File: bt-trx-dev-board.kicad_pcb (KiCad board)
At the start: 2 copper layers, 78 x 68 mm, 59 parts, among them J1 RJ45, J10 JMP_CON_TRX, J11 VOX_IN, J12 VOX_TRX, J2 PTT_BUTTON, J3 PTT_CON, J5 PTT_SEL, J6 I2C, J7 SW1_CON, J8 I2C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

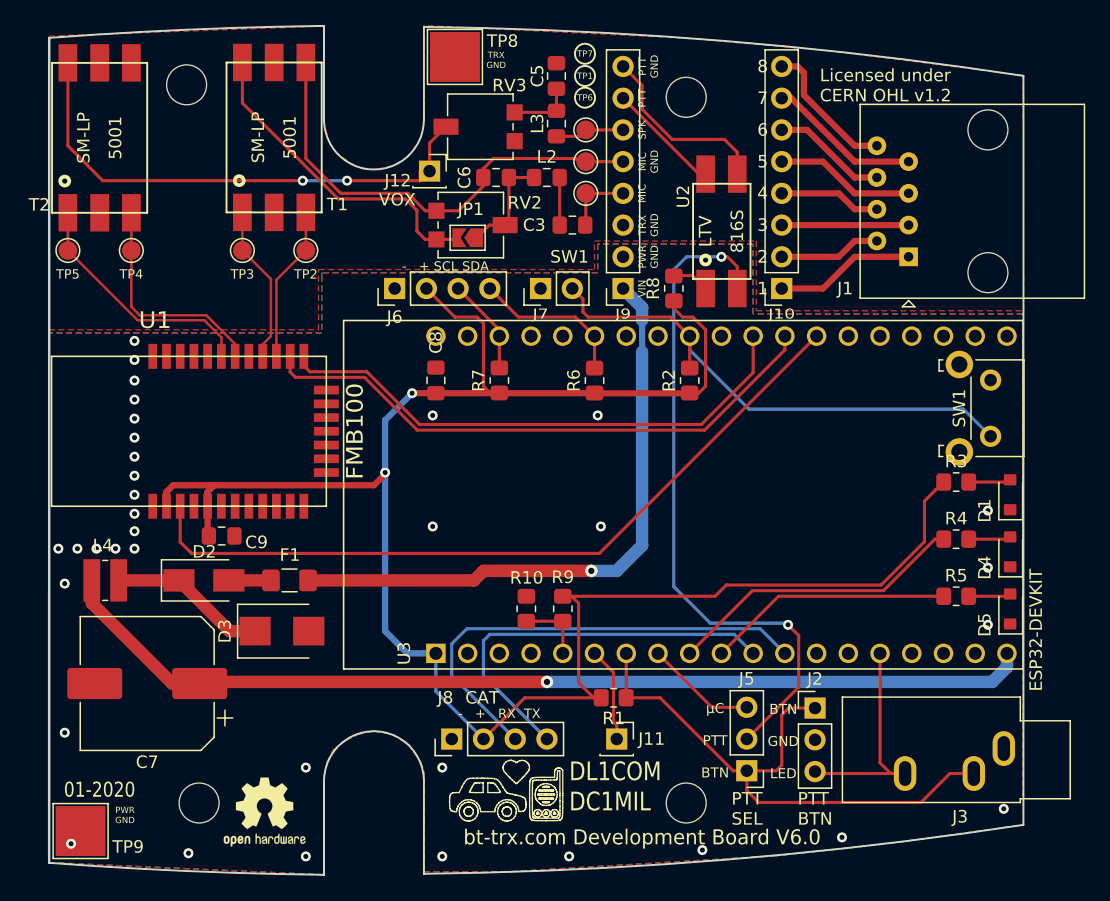
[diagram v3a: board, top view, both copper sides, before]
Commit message: am: Connected FMB100 RST pin to ESP
* Connected FMB100 RST pin to ESP in schematic and PCB
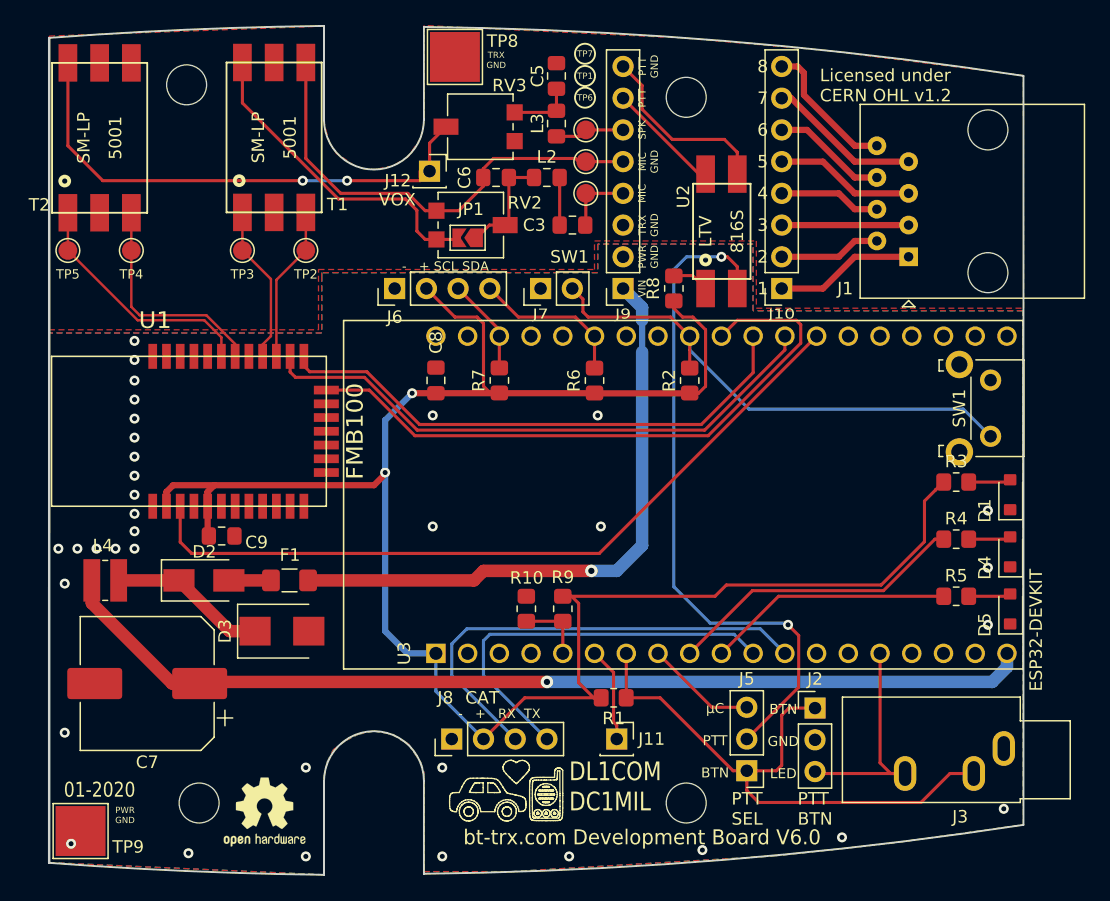
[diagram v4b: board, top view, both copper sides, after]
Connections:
- net /WT32_ONOFF_FROM_UC renamed /FMB_ONOFF_FROM_UC
- U1 pad 19: unconnected-(U1-Pad19) -> /FMB_RST_FROM_UC
- U3 pad 29: unconnected-(U3-Pad29) -> /FMB_RST_FROM_UC
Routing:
- net /FMB_RST_FROM_UC: track 0.00 -> 51.1 mm
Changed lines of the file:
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@@
   (net 2 "+3V3")
   (net 3 "+5V")
-  (net 4 "/WT32_ONOFF_FROM_UC")
+  (net 4 "/FMB_ONOFF_FROM_UC")
   (net 5 "/UART_UC_TX")
   (net 6 "/UART_UC_RX")
@@
   (net 61 "unconnected-(U1-Pad17)")
   (net 62 "unconnected-(U1-Pad18)")
-  (net 63 "unconnected-(U1-Pad19)")
+  (net 63 "/FMB_RST_FROM_UC")
   (net 64 "unconnected-(U1-Pad27)")
   (net 65 "unconnected-(U1-Pad28)")
@@
   (net 75 "unconnected-(U3-Pad24)")
   (net 76 "unconnected-(U3-Pad27)")
-  (net 77 "unconnected-(U3-Pad29)")
-  (net 78 "unconnected-(U3-Pad33)")
-  (net 79 "unconnected-(U3-Pad34)")
-  (net 80 "unconnected-(U3-Pad35)")
-  (net 81 "unconnected-(U3-Pad36)")
-  (net 82 "unconnected-(U3-Pad37)")
-  (net 83 "unconnected-(U3-Pad38)")
-  (net 84 "unconnected-(U1-Pad24)")
+  (net 77 "unconnected-(U3-Pad33)")
+  (net 78 "unconnected-(U3-Pad34)")
+  (net 79 "unconnected-(U3-Pad35)")
+  (net 80 "unconnected-(U3-Pad36)")
+  (net 81 "unconnected-(U3-Pad37)")
+  (net 82 "unconnected-(U3-Pad38)")
+  (net 83 "unconnected-(U1-Pad24)")
   (footprint "MountingHole:MountingHole_3.2mm_M3_DIN965" (layer "F.Cu")
     (at 171.425 127.55)
@@
       (net 10 "/Microcontroller/BTN0") (pinfunction "IO18") (pintype "bidirectional"))
     (pad "29" thru_hole circle locked (at 12.7 3.1 90) (size 1.56 1.56) (drill 1.04) (layers *.Cu *.Mask)
-      (net 77 "unconnected-(U3-Pad29)") (pinfunction "IO5") (pintype "bidirectional+no_connect"))
+      (net 63 "/FMB_RST_FROM_UC") (pinfunction "IO5") (pintype "bidirectional"))
     (pad "30" thru_hole circle locked (at 12.7 5.64 90) (size 1.56 1.56) (drill 1.04) (layers *.Cu *.Mask)
       (net 5 "/UART_UC_TX") (pinfunction "IO17") (pintype "bidirectional"))
@@
       (net 6 "/UART_UC_RX") (pinfunction "IO16") (pintype "bidirectional"))
     (pad "32" thru_hole circle locked (at 12.7 10.72 90) (size 1.56 1.56) (drill 1.04) (layers *.Cu *.Mask)
-      (net 4 "/WT32_ONOFF_FROM_UC") (pinfunction "IO4") (pintype "bidirectional"))
+      (net 4 "/FMB_ONOFF_FROM_UC") (pinfunction "IO4") (pintype "bidirectional"))
     (pad "33" thru_hole circle locked (at 12.7 13.26 90) (size 1.56 1.56) (drill 1.04) (layers *.Cu *.Mask)
-      (net 78 "unconnected-(U3-Pad33)") (pinfunction "IO0") (pintype "bidirectional+no_connect"))
+      (net 77 "unconnected-(U3-Pad33)") (pinfunction "IO0") (pintype "bidirectional+no_connect"))
     (pad "34" thru_hole circle locked (at 12.7 15.8 90) (size 1.56 1.56) (drill 1.04) (layers *.Cu *.Mask)
-      (net 79 "unconnected-(U3-Pad34)") (pinfunction "IO2") (pintype "bidirectional+no_connect"))
+      (net 78 "unconnected-(U3-Pad34)") (pinfunction "IO2") (pintype "bidirectional+no_connect"))
     (pad "35" thru_hole circle locked (at 12.7 18.34 90) (size 1.56 1.56) (drill 1.04) (layers *.Cu *.Mask)
-      (net 80 "unconnected-(U3-Pad35)") (pinfunction "IO15") (pintype "bidirectional+no_connect"))
+      (net 79 "unconnected-(U3-Pad35)") (pinfunction "IO15") (pintype "bidirectional+no_connect"))
     (pad "36" thru_hole circle locked (at 12.7 20.88 90) (size 1.56 1.56) (drill 1.04) (layers *.Cu *.Mask)
-      (net 81 "unconnected-(U3-Pad36)") (pinfunction "SD1") (pintype "bidirectional+no_connect"))
+      (net 80 "unconnected-(U3-Pad36)") (pinfunction "SD1") (pintype "bidirectional+no_connect"))
     (pad "37" thru_hole circle locked (at 12.7 23.42 90) (size 1.56 1.56) (drill 1.04) (layers *.Cu *.Mask)
-      (net 82 "unconnected-(U3-Pad37)") (pinfunction "SD0") (pintype "bidirectional+no_connect"))
+      (net 81 "unconnected-(U3-Pad37)") (pinfunction "SD0") (pintype "bidirectional+no_connect"))
     (pad "38" thru_hole circle locked (at 12.7 25.96 90) (size 1.56 1.56) (drill 1.04) (layers *.Cu *.Mask)
-      (net 83 "unconnected-(U3-Pad38)") (pinfunction "CLK") (pintype "input+no_connect"))
+      (net 82 "unconnected-(U3-Pad38)") (pinfunction "CLK") (pintype "input+no_connect"))
   )
   (footprint "Capacitor_SMD:CP_Elec_10x10.5" (layer "F.Cu")
@@
       (net 2 "+3V3") (pinfunction "VBAT") (pintype "power_in"))
     (pad "3" smd rect locked (at -11.7 0) (size 0.7 2) (layers "F.Cu" "F.Paste" "F.Mask")
-      (net 4 "/WT32_ONOFF_FROM_UC") (pinfunction "VREG_EN") (pintype "bidirectional"))
+      (net 4 "/FMB_ONOFF_FROM_UC") (pinfunction "VREG_EN") (pintype "bidirectional"))
     (pad "4" smd rect locked (at -10.6 0) (size 0.7 2) (layers "F.Cu" "F.Paste" "F.Mask")
       (net 50 "unconnected-(U1-Pad4)") (pinfunction "PIO16") (pintype "bidirectional+no_connect"))
@@
       (net 62 "unconnected-(U1-Pad18)") (pinfunction "PIO3") (pintype "bidirectional+no_connect"))
     (pad "19" smd rect locked (at 0 -9.3 90) (size 0.7 2) (layers "F.Cu" "F.Paste" "F.Mask")
-      (net 63 "unconnected-(U1-Pad19)") (pinfunction "PIO1/RSTN") (pintype "bidirectional+no_connect"))
+      (net 63 "/FMB_RST_FROM_UC") (pinfunction "PIO1/RSTN") (pintype "bidirectional"))
     (pad "20" smd rect locked (at -1.8 -12) (size 0.7 2) (layers "F.Cu" "F.Paste" "F.Mask")
       (net 5 "/UART_UC_TX") (pinfunction "UART_RX") (pintype "bidirectional"))
@@
       (net 24 "/A_OUT_LP") (pinfunction "SPK_P") (pintype "passive"))
     (pad "24" smd rect locked (at -6.2 -12) (size 0.7 2) (layers "F.Cu" "F.Paste" "F.Mask")
-      (net 84 "unconnected-(U1-Pad24)") (pinfunction "MIC_BIAS") (pintype "power_out+no_connect"))
+      (net 83 "unconnected-(U1-Pad24)") (pinfunction "MIC_BIAS") (pintype "power_out+no_connect"))
     (pad "25" smd rect locked (at -7.3 -12) (size 0.7 2) (layers "F.Cu" "F.Paste" "F.Mask")
       (net 25 "/A_IN_LN") (pinfunction "MIC1_N") (pintype "passive"))
@@
   (segment (start 161.544 112.998) (end 161.544 115.57) (width 0.25) (layer "F.Cu") (net 49))
   (segment (start 158.623 112.998) (end 161.544 112.998) (width 0.25) (layer "F.Cu") (net 49))
+  (segment (start 175.514 88.9) (end 180.2384 88.9) (width 0.25) (layer "F.Cu") (net 63))
+  (segment (start 174.244 90.17) (end 175.514 88.9) (width 0.25) (layer "F.Cu") (net 63))
+  (segment (start 180.2384 88.9) (end 180.594 89.2556) (width 0.25) (layer "F.Cu") (net 63))
+  (segment (start 149.704208 98.145) (end 146.049208 94.49) (width 0.25) (layer "F.Cu") (net 63))
+  (segment (start 180.594 90.7288) (end 173.1778 98.145) (width 0.25) (layer "F.Cu") (net 63))
+  (segment (start 146.049208 94.49) (end 142.6112 94.49) (width 0.25) (layer "F.Cu") (net 63))
+  (segment (start 180.594 89.2556) (end 180.594 90.7288) (width 0.25) (layer "F.Cu") (net 63))
+  (segment (start 173.1778 98.145) (end 149.704208 98.145) (width 0.25) (layer "F.Cu") (net 63))
   (zone (net 28) (net_name "GNDPWR") (layer "F.Cu") (hatch edge 0.508)
     (connect_pads (clearance 0.2))
@@
     (polygon
       (pts
-        (xy 198.374 88.392)
-        (xy 176.784 88.392)
+        (xy 198.374 88.138)
+        (xy 176.784 88.138)
         (xy 176.784 82.804)
         (xy 164.338 82.804)
@@
         (xy 164.084 82.55)
         (xy 177.038 82.55)
-        (xy 177.038 88.138)
-        (xy 198.4375 88.138)
+        (xy 177.038 87.9348)
+        (xy 198.4375 87.9348)
       )
     )
@@
     (polygon
       (pts
-        (xy 198.374 88.392)
-        (xy 176.784 88.392)
+        (xy 198.374 88.138)
+        (xy 176.784 88.138)
         (xy 176.784 82.804)
         (xy 164.338 82.804)

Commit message: am: updated date on pcb
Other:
- board text added: "03-2023"
- board text removed: "01-2020"
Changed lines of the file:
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@@
     (effects (font (size 0.75 0.75) (thickness 0.125)))
   )
-  (gr_text "01-2020" (at 124.46 126.492) (layer "F.SilkS")
+  (gr_text "03-2023" (at 124.46 126.492) (layer "F.SilkS")
     (effects (font (size 1.2 1) (thickness 0.15)))
   )
